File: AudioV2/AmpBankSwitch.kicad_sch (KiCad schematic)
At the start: 16 parts, among them U311 TMUX7612, U312 TMUX7612

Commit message: re asighn pin
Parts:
- removed C313, C_IO301: 100nF, Capacitor_SMD:C_1206_3216Metric_Pad1.33x1.80mm_HandSolder, symbol Device:C
- removed H303: M3, MountingHole:MountingHole_3.2mm_M3, symbol Mechanical:MountingHole
- removed J_PWR301: SLOT PWR/CTRL (D18), Connector_PinHeader_2.54mm:PinHeader_2x06_P2.54mm_Vertical, symbol Connector_Generic:Conn_02x06_Odd_Even
- removed U312: TMUX7612, Package_SO:TSSOP-16_4.4x5mm_P0.65mm, symbol AudioV2:TMUX7612
- removed U_IO301: MCP23017, Package_DIP:DIP-28_W7.62mm, symbol Interface_Expansion:MCP23017x-x-SP
- added C314: 100nF, Capacitor_SMD:C_1206_3216Metric_Pad1.33x1.80mm_HandSolder, symbol Device:C
- added C_BULK_N301: 100uF 35V, Capacitor_SMD:CP_Elec_10x12.6, symbol Device:C_Polarized
- added J_PWR301: SLOT PWR/CTRL (D18), Connector_PinHeader_2.54mm:PinHeader_2x08_P2.54mm_Vertical, symbol Connector_Generic:Conn_02x08_Odd_Even
- added U311: TMUX7612, Package_SO:TSSOP-16_4.4x5mm_P0.65mm, symbol AudioV2:TMUX7612
- C313: renamed from U311; value TMUX7612 -> 100nF; footprint Package_SO:TSSOP-16_4.4x5mm_P0.65mm -> Capacitor_SMD:C_1206_3216Metric_Pad1.33x1.80mm_HandSolder; symbol AudioV2:TMUX7612 -> Device:C
- H303: renamed from C314; value 100nF -> M3; footprint Capacitor_SMD:C_1206_3216Metric_Pad1.33x1.80mm_HandSolder -> MountingHole:MountingHole_3.2mm_M3; symbol Device:C -> Mechanical:MountingHole
- U312: renamed from C_BULK_N301; value 100uF 35V -> TMUX7612; footprint Capacitor_SMD:CP_Elec_10x12.6 -> Package_SO:TSSOP-16_4.4x5mm_P0.65mm; symbol Device:C_Polarized -> AudioV2:TMUX7612
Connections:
- net +15V: now also C313.1, U312.13 (VDD), J_PWR301.1 (Pin_1), U311.13 (VDD); no longer C313.13 (VDD)
- net -15V: now also U312.4 (VSS), C314.2, C_BULK_N301.2, J_PWR301.3 (Pin_3), U311.4 (VSS); no longer C313.4 (VSS), H303.2, U312.2
- net AMP_SEL_L: now also U312.10 (D3), U312.7 (D4), U311.10 (D3), U311.7 (D4); no longer C313.10 (D3), C313.7 (D4)
- net AMP_SEL_R: now also U312.15 (D2), U312.2 (D1), U311.15 (D2), U311.2 (D1); no longer C313.15 (D2), C313.2 (D1)
- net A_GND: now also C313.2, U312.5 (GND), C314.1, C_BULK_N301.1, J_PWR301.2 (Pin_2), J_PWR301.4 (Pin_4), U311.5 (GND); no longer C313.5 (GND), H303.1, U312.1
- net CH1_OUT_L: now also U311.6 (S4); no longer C313.6 (S4)
- net CH1_OUT_R: now also U311.3 (S1); no longer C313.3 (S1)
- net CH2_OUT_L: now also U311.11 (S3); no longer C313.11 (S3)
- net CH2_OUT_R: now also U311.14 (S2); no longer C313.14 (S2)
- net CH3_OUT_L: now also U312.6 (S4)
- net CH3_OUT_R: now also U312.3 (S1)
- net CH4_OUT_L: now also U312.11 (S3)
- net CH4_OUT_R: now also U312.14 (S2)
- net SEL_CH1: now also J_PWR301.13 (Pin_13), U311.1 (SEL1), U311.8 (SEL4); no longer C313.1 (SEL1), C313.8 (SEL4)
- net SEL_CH2: now also J_PWR301.15 (Pin_15), U311.16 (SEL2), U311.9 (SEL3); no longer C313.16 (SEL2), C313.9 (SEL3)
- net SEL_CH3: now also U312.1 (SEL1), U312.8 (SEL4), J_PWR301.14 (Pin_14)
- net SEL_CH4: now also U312.16 (SEL2), U312.9 (SEL3), J_PWR301.16 (Pin_16)
- no-connect marks 20 -> 10

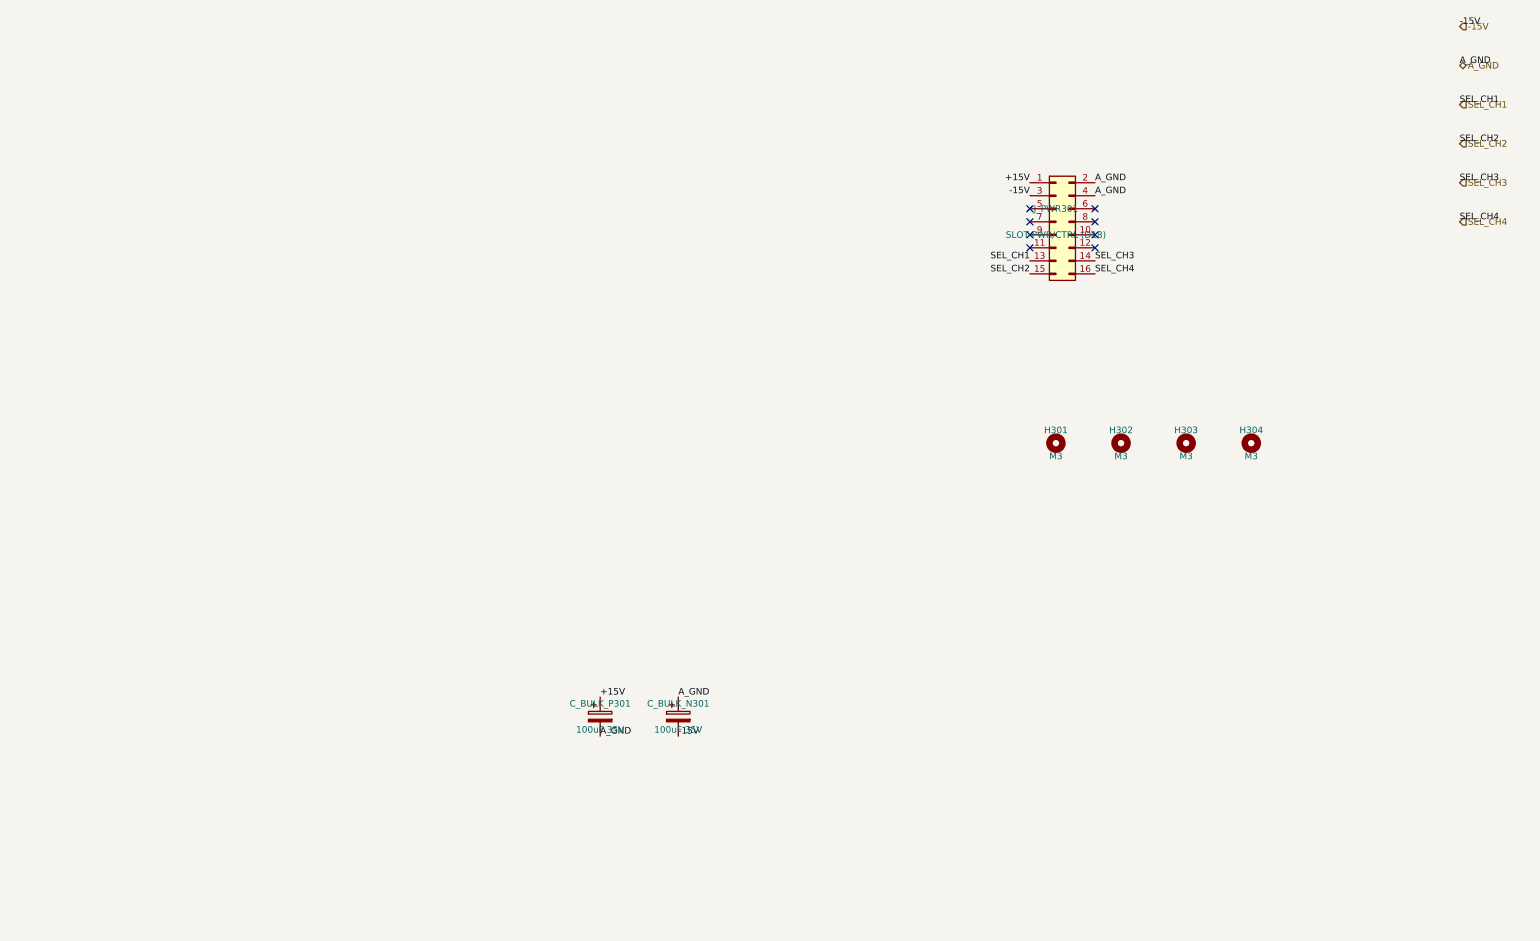
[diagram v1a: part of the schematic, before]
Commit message: AudioV2: AmpBank 番地をジャンパ 6 段へ（縦積み向け）
スロット側 ADDR（D21）をやめ、娘の A0/A1/A2 ソルダージャンパで
0x20/21/23/24/25/26 を選択。スイッチ版にも MCP を載せ SEL を現地駆動し、
親 U_IO101 を廃止。コネクタ pin11–16 は N.C.。

Co-authored-by: m_arino <indare@users.noreply.github.com>
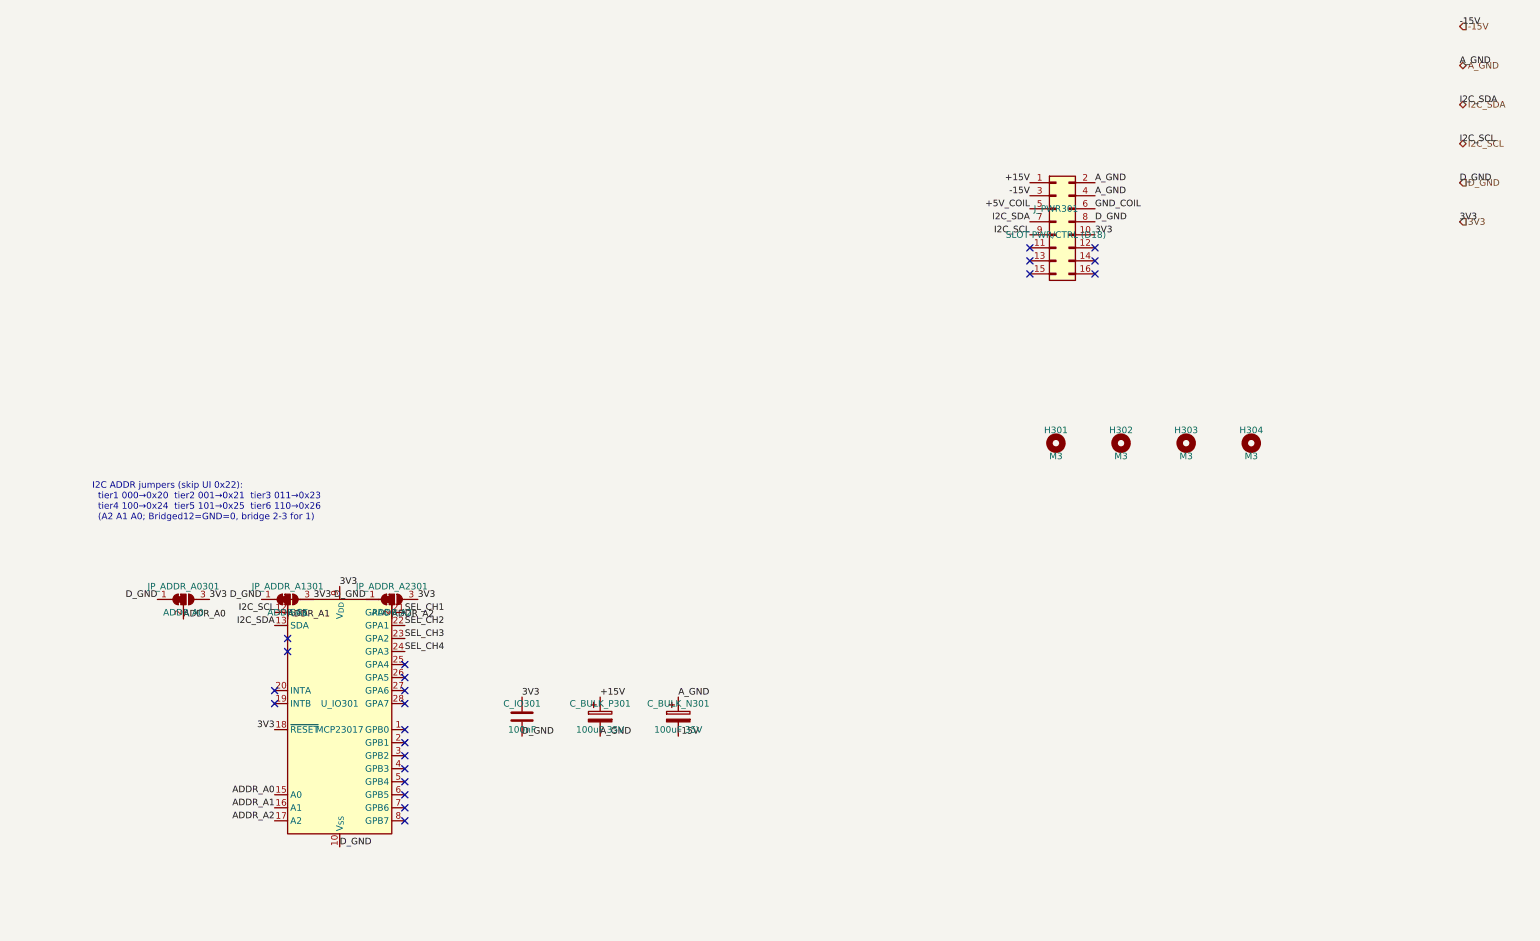
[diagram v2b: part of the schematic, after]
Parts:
- removed U312: TMUX7612, Package_SO:TSSOP-16_4.4x5mm_P0.65mm, symbol AudioV2:TMUX7612
- added C_IO301: 100nF, Capacitor_SMD:C_1206_3216Metric_Pad1.33x1.80mm_HandSolder, symbol Device:C
- added H302: M3, MountingHole:MountingHole_3.2mm_M3, symbol Mechanical:MountingHole
- added JP_ADDR_A0301: ADDR A0, Jumper:SolderJumper-3_P1.3mm_Bridged12_Pad1.0x1.5mm_NumberLabels, symbol Jumper:SolderJumper_3_Bridged12
- added JP_ADDR_A1301: ADDR A1, Jumper:SolderJumper-3_P1.3mm_Bridged12_Pad1.0x1.5mm_NumberLabels, symbol Jumper:SolderJumper_3_Bridged12
- added JP_ADDR_A2301: ADDR A2, Jumper:SolderJumper-3_P1.3mm_Bridged12_Pad1.0x1.5mm_NumberLabels, symbol Jumper:SolderJumper_3_Bridged12
- added U_IO301: MCP23017, Package_DIP:DIP-28_W7.62mm, symbol Interface_Expansion:MCP23017x-x-SP
- U312: renamed from H302; value M3 -> TMUX7612; footprint MountingHole:MountingHole_3.2mm_M3 -> Package_SO:TSSOP-16_4.4x5mm_P0.65mm; symbol Mechanical:MountingHole -> AudioV2:TMUX7612
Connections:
- net +15V: now also U312.13 (VDD)
- net -15V: now also U312.4 (VSS)
- net AMP_SEL_L: now also U312.10 (D3), U312.7 (D4)
- net AMP_SEL_R: now also U312.15 (D2), U312.2 (D1)
- net A_GND: now also U312.5 (GND)
- net CH3_OUT_L: now also U312.6 (S4)
- net CH3_OUT_R: now also U312.3 (S1)
- net CH4_OUT_L: now also U312.11 (S3)
- net CH4_OUT_R: now also U312.14 (S2)
- net SEL_CH1: now also U_IO301.21 (GPA0); no longer J_PWR301.13 (Pin_13)
- net SEL_CH2: now also U_IO301.22 (GPA1); no longer J_PWR301.15 (Pin_15)
- net SEL_CH3: now also U312.1 (SEL1), U312.8 (SEL4), U_IO301.23 (GPA2); no longer J_PWR301.14 (Pin_14)
- net SEL_CH4: now also U312.16 (SEL2), U312.9 (SEL3), U_IO301.24 (GPA3); no longer J_PWR301.16 (Pin_16)
- net 3V3: now reaches J_PWR301.10 (Pin_10)
- net 3V3: now also C_IO301.1, JP_ADDR_A0301.3 (B), JP_ADDR_A1301.3 (B), JP_ADDR_A2301.3 (B), U_IO301.18 (~{RESET}), U_IO301.9 (V_{DD})
- net +5V_COIL: now reaches J_PWR301.5 (Pin_5)
- net GND_COIL: now reaches J_PWR301.6 (Pin_6)
- net I2C_SDA: now reaches J_PWR301.7 (Pin_7)
- net I2C_SDA: now also U_IO301.13 (SDA)
- net D_GND: now reaches J_PWR301.8 (Pin_8)
- net D_GND: now also C_IO301.2, JP_ADDR_A0301.1 (A), JP_ADDR_A1301.1 (A), JP_ADDR_A2301.1 (A), U_IO301.10 (V_{SS})
- net I2C_SCL: now reaches J_PWR301.9 (Pin_9)
- net I2C_SCL: now also U_IO301.12 (SCK)
- new net ADDR_A0: JP_ADDR_A0301.2 (C), U_IO301.15 (A0)
- new net ADDR_A1: JP_ADDR_A1301.2 (C), U_IO301.16 (A1)
- new net ADDR_A2: JP_ADDR_A2301.2 (C), U_IO301.17 (A2)
- no-connect marks 10 -> 24
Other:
- note added: "I2C ADDR jumpers (skip UI 0x22): tier1 000→0x20 tier2 001→0x21 tier3 011→0x23 tier4 100→0x24 tier5 101→0x25 tier6 110→0x26 (A2 A1 A0; Bridged12=GND=0, bridge 2-3 for 1)"
